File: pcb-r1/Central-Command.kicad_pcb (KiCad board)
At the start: 4 copper layers, 16 parts, among them P1 CONN_01X06, P2 CONN_01X02, U1 STM32F030C8, U2 MCP1700T-3302E

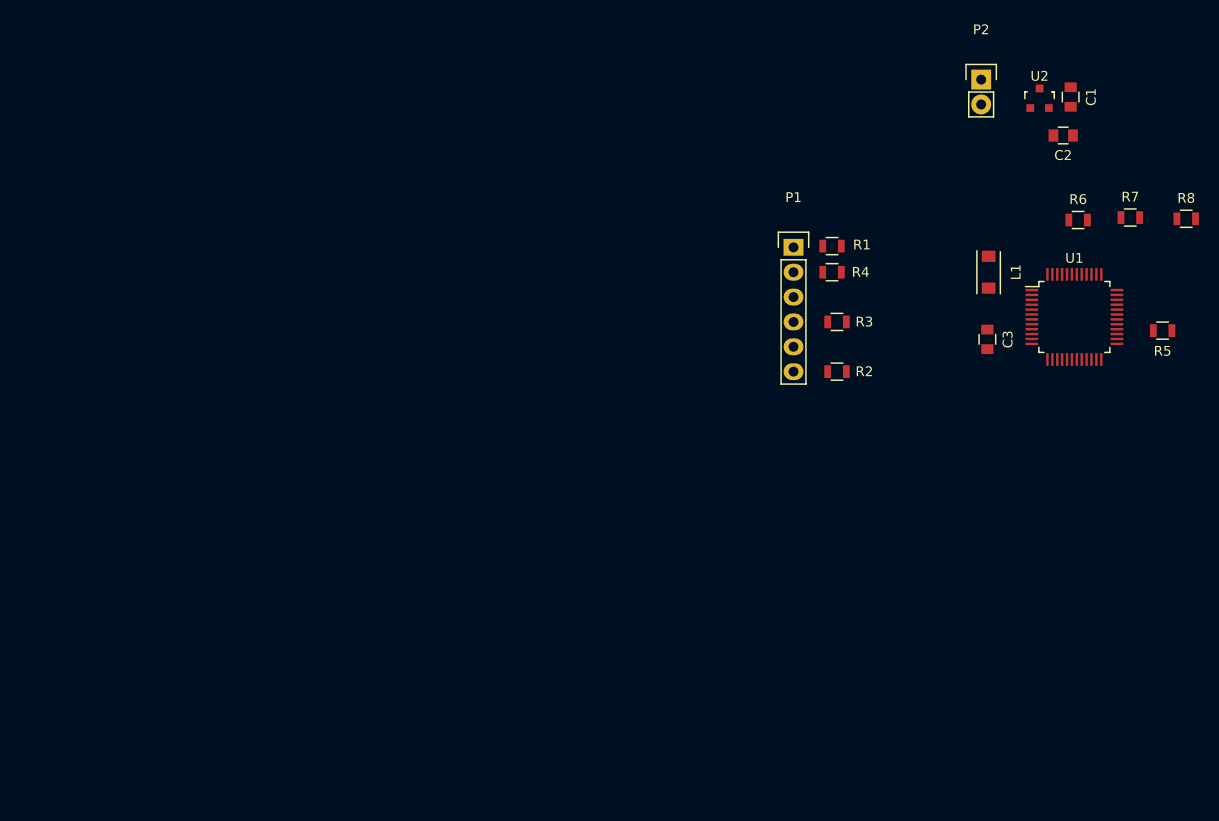
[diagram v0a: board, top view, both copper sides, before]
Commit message: Started preliminary layout of the parts
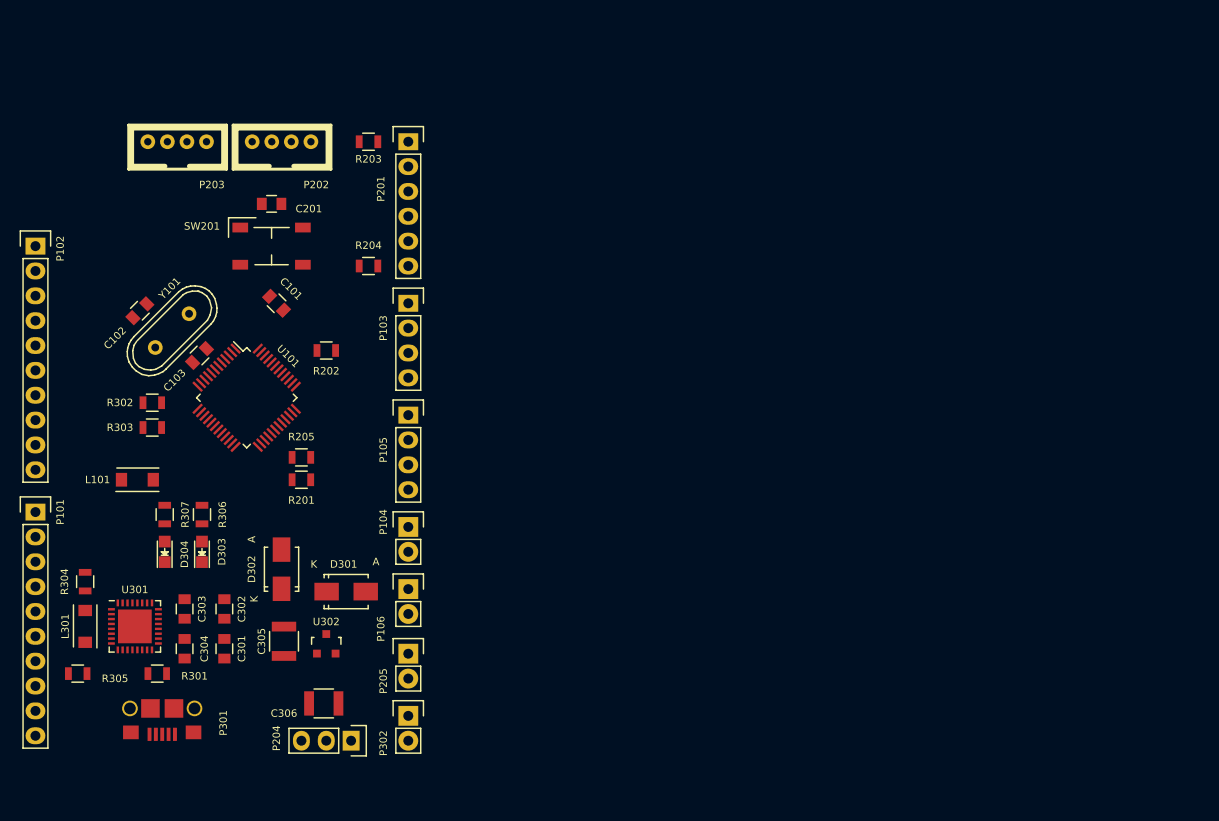
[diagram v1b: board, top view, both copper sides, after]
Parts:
- removed C1, C2: 1μF, Capacitors_SMD:C_0805
- removed C3: C, Capacitors_SMD:C_0805
- removed L1: INDUCTOR, Inductors_NEOSID:Neosid_Inductor_SM1206
- removed P1: CONN_01X06, Pin_Headers:Pin_Header_Straight_1x06
- removed P2: CONN_01X02, Pin_Headers:Pin_Header_Straight_1x02
- removed R1, R2: 0Ω, Resistors_SMD:R_0805
- removed R3, R4, R5, R6, R7, R8: R, Resistors_SMD:R_0805
- removed U1: STM32F030C8, Housings_QFP:LQFP-48_7x7mm_Pitch0.5mm
- removed U2: MCP1700T-3302E, Housings_SOT-23_SOT-143_TSOT-6:SOT-23
- added C101: C, Capacitors_SMD:C_0805, F.Cu at (98.0, 88.9)
- added C102: 20pF, Capacitors_SMD:C_0805, F.Cu at (84.1, 89.7)
- added C103: 20pF, Capacitors_SMD:C_0805, F.Cu at (90.2, 94.2)
- added C201: C, Capacitors_SMD:C_0805, F.Cu at (97.5, 78.7)
- added C301: 0.01μF, Capacitors_SMD:C_0805, F.Cu at (92.7, 124.2)
- added C302: 0.1μF, Capacitors_SMD:C_0805, F.Cu at (92.7, 120.1)
- added C303: 4.7μF, Capacitors_SMD:C_0805, F.Cu at (88.6, 120.1)
- added C304: 0.1μF, Capacitors_SMD:C_0805, F.Cu at (88.6, 124.2)
- added C305: 10μF, Capacitors_SMD:C_1210, F.Cu at (98.8, 123.4)
- added C306: 10μF, Capacitors_SMD:C_1210, F.Cu at (102.9, 129.8)
- added D301: D_Schottky, Diodes_SMD:SMA_Standard, F.Cu at (105.2, 118.4)
- added D302: D_Schottky, Diodes_SMD:SMA_Standard, F.Cu at (98.6, 116.1)
- added D303: LED, LEDs:LED-0805, F.Cu at (90.4, 114.3)
- added D304: LED, LEDs:LED-0805, F.Cu at (86.6, 114.3)
- added L101: INDUCTOR, Inductors_NEOSID:Neosid_Inductor_SM1206, F.Cu at (83.8, 106.9)
- added L301: FERRITE, Inductors_NEOSID:Neosid_Inductor_SM1206, F.Cu at (78.5, 121.9)
- added P101: CONN_01X10, Pin_Headers:Pin_Header_Straight_1x10, F.Cu at (73.4, 110.2)
- added P102: CONN_01X10, Pin_Headers:Pin_Header_Straight_1x10, F.Cu at (73.4, 83.1)
- added P103: CONN_01X04, Pin_Headers:Pin_Header_Straight_1x04, F.Cu at (111.5, 88.9)
- added P104: CONN_01X02, Pin_Headers:Pin_Header_Straight_1x02, F.Cu at (111.5, 111.8)
- added P105: CONN_01X04, Pin_Headers:Pin_Header_Straight_1x04, F.Cu at (111.5, 100.3)
- added P106: CONN_01X02, Pin_Headers:Pin_Header_Straight_1x02, F.Cu at (111.5, 118.1)
- added P201: CONN_01X06, Pin_Headers:Pin_Header_Straight_1x06, F.Cu at (111.5, 72.4)
- added P202: CONN_01X04, CentralCommand:Grove-2mm, F.Cu at (95.5, 72.4)
- added P203: CONN_01X04, CentralCommand:Grove-2mm, F.Cu at (84.8, 72.4)
- added P204: CONN_01X03, Pin_Headers:Pin_Header_Straight_1x03, F.Cu at (105.7, 133.6)
- added P205: CONN_01X02, Pin_Headers:Pin_Header_Straight_1x02, F.Cu at (111.5, 124.7)
- added P301: USB-MICRO-B, CentralCommand:USB_Micro_B, F.Cu at (86.4, 130.3)
- added P302: CONN_01X02, Pin_Headers:Pin_Header_Straight_1x02, F.Cu at (111.5, 131.1)
- added R201: R, Resistors_SMD:R_0805, F.Cu at (100.6, 106.9)
- added R202: R, Resistors_SMD:R_0805, F.Cu at (103.1, 93.7)
- added R203: 0Ω, Resistors_SMD:R_0805, F.Cu at (107.4, 72.4)
- added R204: 0Ω, Resistors_SMD:R_0805, F.Cu at (107.4, 85.1)
- added R205: R, Resistors_SMD:R_0805, F.Cu at (100.6, 104.6)
- added R301: 0Ω, Resistors_SMD:R_0805, F.Cu at (85.9, 126.7)
- added R302: 0Ω, Resistors_SMD:R_0805, F.Cu at (85.3, 99.1)
- added R303: 0Ω, Resistors_SMD:R_0805, F.Cu at (85.3, 101.6)
- added R304: NOPE, Resistors_SMD:R_0805, F.Cu at (78.5, 117.3)
- added R305: NOPE, Resistors_SMD:R_0805, F.Cu at (77.7, 126.7)
- added R306: 270Ω, Resistors_SMD:R_0805, F.Cu at (90.4, 110.5)
- added R307: 270Ω, Resistors_SMD:R_0805, F.Cu at (86.6, 110.5)
- added SW201: SW_PUSH, CentralCommand:PTS525SM15SMTR2LFS, F.Cu at (97.5, 83.1)
- added U101: STM32F030C8, Housings_QFP:LQFP-48_7x7mm_Pitch0.5mm, F.Cu at (95.0, 98.6)
- added U301: FT232RQ, Housings_DFN_QFN:QFN-32-1EP_5x5mm_Pitch0.5mm, F.Cu at (83.6, 121.9)
- added U302: MCP1700T-3302E, TO_SOT_Packages_SMD:SOT-23, F.Cu at (103.1, 123.7)
- added Y101: Crystal, Crystals:Crystal_HC49-U_Vertical, F.Cu at (87.4, 91.7)

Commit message: New initial layout
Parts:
- added REF**: MountingHole_3mm, Mounting_Holes:MountingHole_3mm, F.Cu at (111.0, 79.5)
- added REF**: MountingHole_3mm, Mounting_Holes:MountingHole_3mm, F.Cu at (79.5, 79.5)
- added REF**: MountingHole_3mm, Mounting_Holes:MountingHole_3mm, F.Cu at (79.5, 136.4)
- added REF**: MountingHole_3mm, Mounting_Holes:MountingHole_3mm, F.Cu at (111.0, 136.4)
- moved P202 53.8 mm to (79.2, 123.7), turned to 270 degrees
- moved P204 50.8 mm to (107.2, 82.8)
- moved P203 41.3 mm to (79.2, 113.3), turned to 270 degrees
- moved P205 35.5 mm to (82.8, 103.9)
- moved P101 33.7 mm to (84.1, 78.2), turned to 90 degrees
- moved SW201 32.8 mm to (103.4, 115.3)
- moved C201 32.5 mm to (103.1, 110.7)
- moved P106 27.8 mm to (104.6, 91.2), turned to 225 degrees
- moved R204 23.6 mm to (108.2, 108.7)
- moved R203 23.4 mm to (108.2, 95.8)
- moved P201 23.1 mm to (112.0, 95.5)
- moved P105 11.9 mm to (112.0, 112.3)
- moved P104 9.57 mm to (108.0, 102.9)
- moved R305 9.55 mm to (86.1, 131.3)
- moved R306 8.27 mm to (91.9, 118.6), turned to 0 degrees
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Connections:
- L101 pad 1: 3V3 -> /Comm/PWR
- U101 pad 1: 3V3 -> /Comm/PWR
- U101 pad 24: 3V3 -> /Comm/PWR
- U101 pad 48: 3V3 -> /Comm/PWR
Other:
- board outline added: 38.1 x 63.5 mm
- net class Default: clearance 0.2 -> 0.1524; trace_width 0.25 -> 0.1524; via_dia 0.6 -> 0.6858; via_drill 0.4 -> 0.3302
- rule trace_clearance: 0.2 -> 0.1524
- rule trace_min: 0.2 -> 0.1524
- rule via_min_drill: 0.3 -> 0.3302
- rule via_min_size: 0.4 -> 0.6858

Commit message: Corrected the symbol and footprint for the reset switch
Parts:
- SW201: value SW_PUSH -> TL3315NF160Q
- moved P202 4.68 mm to (78.2, 128.3), turned to 90 degrees
- moved P203 4.44 mm to (78.2, 117.6), turned to 90 degrees
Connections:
- P103 pad 3: /SPI_MISO -> (no net)
- P103 pad 4: /SPI_MOSI -> (no net)
- P104 pad 2: /I2C1_SCL -> (no net)
- P203 pad 1: GND -> /Comm/SDA
- P203 pad 2: /Comm/PWR -> /Comm/SCL
- P203 pad 3: /Comm/SCL -> /Comm/PWR
- P203 pad 4: /Comm/SDA -> GND
- P301 pad 4: Net-(P301-Pad4) -> (no net)
- R204 pad 1: /Comm/TRACE -> (no net)
- R301 pad 2: NRST -> (no net)
- SW201 pad 2: GND -> /Comm/NRST
- SW201 pad 3: (no net) -> GND
- SW201 pad 4: (no net) -> GND
- U101 pad 36: /I2C1_SLK -> (no net)
- U101 pad 40: /SPI1_MISO -> (no net)
- U101 pad 41: /SPI1_MOSI -> (no net)
- U301 pad 10: Net-(U301-Pad10) -> (no net)
- U301 pad 11: Net-(U301-Pad11) -> (no net)
- U301 pad 12: Net-(U301-Pad12) -> (no net)
- U301 pad 13: Net-(U301-Pad13) -> (no net)
- U301 pad 23: Net-(U301-Pad23) -> (no net)
- U301 pad 25: Net-(U301-Pad25) -> (no net)
- U301 pad 27: Net-(U301-Pad27) -> (no net)
- U301 pad 28: Net-(U301-Pad28) -> (no net)
- U301 pad 29: Net-(U301-Pad29) -> (no net)
- U301 pad 3: Net-(U301-Pad3) -> (no net)
- U301 pad 31: Net-(U301-Pad31) -> (no net)
- U301 pad 5: Net-(U301-Pad5) -> (no net)
- U301 pad 6: Net-(U301-Pad6) -> (no net)
- U301 pad 7: Net-(U301-Pad7) -> (no net)
- U301 pad 9: Net-(U301-Pad9) -> (no net)

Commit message: Updates to the PCB
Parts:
- moved P104 21.1 mm to (112.0, 123.6)
- moved C101 8.81 mm to (90.3, 94.7), turned to 45 degrees
- moved C102 8.36 mm to (91.1, 84.5), turned to 315 degrees
- moved L101 2.93 mm to (82.7, 99.2)
- moved Y101 2.64 mm to (90.0, 88.6), turned to 315 degrees
- moved C103 1.98 mm to (94.0, 87.2), turned to 135 degrees
- moved P105 0.51 mm to (112.0, 111.8)
- moved P302 0.40 mm to (112.0, 129.9)
- moved R203 0.28 mm to (108.1, 95.5), turned to 180 degrees
- moved P201 0.25 mm to (112.0, 95.2)
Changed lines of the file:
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@@
-(kicad_pcb (version 4) (host pcbnew 4.0.0-stable)
+(kicad_pcb (version 4) (host pcbnew 4.0.0-2.201512072331+6194~38~ubuntu14.04.1-stable)
   (general
     (links 123)
@@
   )
   (module Capacitors_SMD:C_0805 (layer F.Cu)
-    (at 92.583 86.233)
+    (at 90.297 94.742 45)
     (descr "Capacitor SMD 0805, reflow soldering, AVX (see smccp.pdf)")
     (tags "capacitor 0805")
     (attr smd)
-    (fp_text reference C101 (at 0 -2.1) (layer F.SilkS)
-      (effects (font (size 0.762 0.762) (thickness 0.127)))
-    )
-    (fp_text value C (at 0 2.1) (layer F.Fab)
+    (fp_text reference C101 (at 0 -2.1 45) (layer F.SilkS)
+      (effects (font (size 0.762 0.762) (thickness 0.127)))
+    )
+    (fp_text value C (at 0 2.1 45) (layer F.Fab)
       (effects (font (size 0.762 0.762) (thickness 0.127)))
     )
@@
     (fp_line (start 0.5 -0.85) (end -0.5 -0.85) (layer F.SilkS) (width 0.15))
     (fp_line (start -0.5 0.85) (end 0.5 0.85) (layer F.SilkS) (width 0.15))
-    (pad 1 smd rect (at -1 0) (size 1 1.25) (layers F.Cu F.Paste F.Mask)
+    (pad 1 smd rect (at -1 0 45) (size 1 1.25) (layers F.Cu F.Paste F.Mask)
       (net 1 "Net-(C101-Pad1)"))
-    (pad 2 smd rect (at 1 0) (size 1 1.25) (layers F.Cu F.Paste F.Mask)
+    (pad 2 smd rect (at 1 0 45) (size 1 1.25) (layers F.Cu F.Paste F.Mask)
       (net 2 GND))
     (model Capacitors_SMD.3dshapes/C_0805.wrl
@@
   )
   (module Capacitors_SMD:C_0805 (layer F.Cu)
-    (at 83.82 88.646 270)
+    (at 91.059 84.455 315)
     (descr "Capacitor SMD 0805, reflow soldering, AVX (see smccp.pdf)")
     (tags "capacitor 0805")
     (attr smd)
-    (fp_text reference C102 (at -3.771708 0.179605 270) (layer F.SilkS)
-      (effects (font (size 0.762 0.762) (thickness 0.127)))
-    )
-    (fp_text value 20pF (at 0 2.1 270) (layer F.Fab)
+    (fp_text reference C102 (at -0.089803 -1.706249 315) (layer F.SilkS)
+      (effects (font (size 0.762 0.762) (thickness 0.127)))
+    )
+    (fp_text value 20pF (at 0 2.1 315) (layer F.Fab)
       (effects (font (size 0.762 0.762) (thickness 0.127)))
     )
@@
     (fp_line (start 0.5 -0.85) (end -0.5 -0.85) (layer F.SilkS) (width 0.15))
     (fp_line (start -0.5 0.85) (end 0.5 0.85) (layer F.SilkS) (width 0.15))
-    (pad 1 smd rect (at -1 0 270) (size 1 1.25) (layers F.Cu F.Paste F.Mask)
+    (pad 1 smd rect (at -1 0 315) (size 1 1.25) (layers F.Cu F.Paste F.Mask)
       (net 3 "Net-(C102-Pad1)"))
-    (pad 2 smd rect (at 1 0 270) (size 1 1.25) (layers F.Cu F.Paste F.Mask)
+    (pad 2 smd rect (at 1 0 315) (size 1 1.25) (layers F.Cu F.Paste F.Mask)
       (net 2 GND))
     (model Capacitors_SMD.3dshapes/C_0805.wrl
@@
   )
   (module Capacitors_SMD:C_0805 (layer F.Cu)
-    (at 92.583 88.646)
+    (at 93.98 87.249 135)
     (descr "Capacitor SMD 0805, reflow soldering, AVX (see smccp.pdf)")
     (tags "capacitor 0805")
     (attr smd)
-    (fp_text reference C103 (at 3.592102 0) (layer F.SilkS)
-      (effects (font (size 0.762 0.762) (thickness 0.127)))
-    )
-    (fp_text value 20pF (at 0 2.1) (layer F.Fab)
+    (fp_text reference C103 (at 0.089803 1.885854 135) (layer F.SilkS)
+      (effects (font (size 0.762 0.762) (thickness 0.127)))
+    )
+    (fp_text value 20pF (at 0 2.1 135) (layer F.Fab)
       (effects (font (size 0.762 0.762) (thickness 0.127)))
     )
@@
     (fp_line (start 0.5 -0.85) (end -0.5 -0.85) (layer F.SilkS) (width 0.15))
     (fp_line (start -0.5 0.85) (end 0.5 0.85) (layer F.SilkS) (width 0.15))
-    (pad 1 smd rect (at -1 0) (size 1 1.25) (layers F.Cu F.Paste F.Mask)
+    (pad 1 smd rect (at -1 0 135) (size 1 1.25) (layers F.Cu F.Paste F.Mask)
       (net 4 "Net-(C103-Pad1)"))
-    (pad 2 smd rect (at 1 0) (size 1 1.25) (layers F.Cu F.Paste F.Mask)
+    (pad 2 smd rect (at 1 0 135) (size 1 1.25) (layers F.Cu F.Paste F.Mask)
       (net 2 GND))
     (model Capacitors_SMD.3dshapes/C_0805.wrl
@@
     (tags "capacitor 0805")
     (attr smd)
-    (fp_text reference C201 (at 3.81 0.508) (layer F.SilkS)
+    (fp_text reference C201 (at 0.127 -1.778) (layer F.SilkS)
       (effects (font (size 0.762 0.762) (thickness 0.127)))
     )
@@
   )
   (module Inductors_NEOSID:Neosid_Inductor_SM1206 (layer F.Cu)
-    (at 85.598 98.933 90)
+    (at 82.677 99.187 90)
     (descr "Neosid, Inductor, SM1206, Festinduktivitaet, SMD,")
     (tags "Neosid, Inductor, SM1206, Festinduktivitaet, SMD,")
@@
   )
   (module Pin_Headers:Pin_Header_Straight_1x02 (layer F.Cu)
-    (at 107.95 102.87)
+    (at 112.014 123.571)
     (descr "Through hole pin header")
     (tags "pin header")
@@
   )
   (module Pin_Headers:Pin_Header_Straight_1x04 (layer F.Cu)
-    (at 112.014 112.268)
+    (at 112.014 111.76)
     (descr "Through hole pin header")
     (tags "pin header")
@@
   )
   (module Pin_Headers:Pin_Header_Straight_1x06 (layer F.Cu)
-    (at 112.014 95.504)
+    (at 112.014 95.25)
     (descr "Through hole pin header")
     (tags "pin header")
-    (fp_text reference P201 (at -2.794 4.826 90) (layer F.SilkS)
+    (fp_text reference P201 (at -2.413 2.921 90) (layer F.SilkS)
       (effects (font (size 0.762 0.762) (thickness 0.127)))
     )
@@
   )
   (module Pin_Headers:Pin_Header_Straight_1x02 (layer F.Cu)
-    (at 112.141 129.54)
+    (at 112.014 129.921)
     (descr "Through hole pin header")
     (tags "pin header")
@@
   )
   (module Resistors_SMD:R_0805 (layer F.Cu)
-    (at 108.204 95.758)
+    (at 108.077 95.504 180)
     (descr "Resistor SMD 0805, reflow soldering, Vishay (see dcrcw.pdf)")
     (tags "resistor 0805")
     (attr smd)
-    (fp_text reference R203 (at 0 1.778) (layer F.SilkS)
-      (effects (font (size 0.762 0.762) (thickness 0.127)))
-    )
-    (fp_text value 0Ω (at 0 2.1) (layer F.Fab)
+    (fp_text reference R203 (at 0 1.778 180) (layer F.SilkS)
+      (effects (font (size 0.762 0.762) (thickness 0.127)))
+    )
+    (fp_text value 0Ω (at 0 2.1 180) (layer F.Fab)
       (effects (font (size 0.762 0.762) (thickness 0.127)))
     )
@@
     (fp_line (start 0.6 0.875) (end -0.6 0.875) (layer F.SilkS) (width 0.15))
     (fp_line (start -0.6 -0.875) (end 0.6 -0.875) (layer F.SilkS) (width 0.15))
-    (pad 1 smd rect (at -0.95 0) (size 0.7 1.3) (layers F.Cu F.Paste F.Mask)
+    (pad 1 smd rect (at -0.95 0 180) (size 0.7 1.3) (layers F.Cu F.Paste F.Mask)
       (net 44 "Net-(P201-Pad1)"))
-    (pad 2 smd rect (at 0.95 0) (size 0.7 1.3) (layers F.Cu F.Paste F.Mask)
+    (pad 2 smd rect (at 0.95 0 180) (size 0.7 1.3) (layers F.Cu F.Paste F.Mask)
       (net 10 /Comm/PWR))
     (model Resistors_SMD.3dshapes/R_0805.wrl
@@
     (tags "resistor 0805")
     (attr smd)
-    (fp_text reference R204 (at 0 -2.1) (layer F.SilkS)
+    (fp_text reference R204 (at 0.381 1.778) (layer F.SilkS)
       (effects (font (size 0.762 0.762) (thickness 0.127)))
     )
@@
   (module CentralCommand:PTS525SM15SMTR2LFS (layer F.Cu)
     (at 103.378 115.316)
-    (fp_text reference SW201 (at -7.112 -2.032) (layer F.SilkS)
+    (fp_text reference SW201 (at -5.08 0 90) (layer F.SilkS)
       (effects (font (size 0.762 0.762) (thickness 0.127)))
     )
@@
   )
   (module Crystals:Crystal_HC49-U_Vertical (layer F.Cu)
-    (at 87.884 90.17 270)
+    (at 90.043 88.646 315)
     (descr "Crystal, Quarz, HC49/U, vertical, stehend,")
     (tags "Crystal, Quarz, HC49/U, vertical, stehend,")
-    (fp_text reference Y101 (at 2.873682 -3.232892 270) (layer F.SilkS)
-      (effects (font (size 0.762 0.762) (thickness 0.127)))
-    )
-    (fp_text value Crystal (at 0 3.81 270) (layer F.Fab)
+    (fp_text reference Y101 (at 0.089803 3.322695 315) (layer F.SilkS)
+      (effects (font (size 0.762 0.762) (thickness 0.127)))
+    )
+    (fp_text value Crystal (at 0 3.81 315) (layer F.Fab)
       (effects (font (size 0.762 0.762) (thickness 0.127)))
     )
@@
     (fp_line (start 3.6703 2.29108) (end 4.16052 2.1209) (layer F.SilkS) (width 0.15))
     (fp_line (start -3.2004 -2.32918) (end 3.2512 -2.32918) (layer F.SilkS) (width 0.15))
-    (pad 1 thru_hole circle (at -2.44094 0 270) (size 1.50114 1.50114) (drill 0.8001) (layers *.Cu *.Mask F.SilkS)
+    (pad 1 thru_hole circle (at -2.44094 0 315) (size 1.50114 1.50114) (drill 0.8001) (layers *.Cu *.Mask F.SilkS)
       (net 3 "Net-(C102-Pad1)"))
-    (pad 2 thru_hole circle (at 2.44094 0 270) (size 1.50114 1.50114) (drill 0.8001) (layers *.Cu *.Mask F.SilkS)
+    (pad 2 thru_hole circle (at 2.44094 0 315) (size 1.50114 1.50114) (drill 0.8001) (layers *.Cu *.Mask F.SilkS)
       (net 4 "Net-(C103-Pad1)"))
   )
